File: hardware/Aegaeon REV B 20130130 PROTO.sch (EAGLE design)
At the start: 39 parts, among them IC1 ATTINY84A-MMH, Q1 DMN65D8LDW, U1 V_REG_LDOSMD

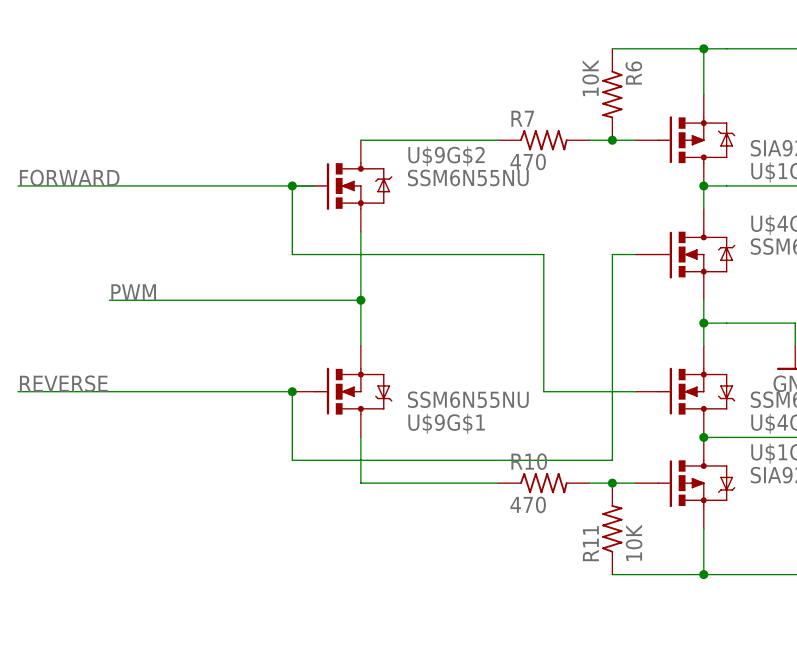
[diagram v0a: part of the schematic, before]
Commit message: Updated proto schematics to match new bridge design. Streamlined design in simulation file.
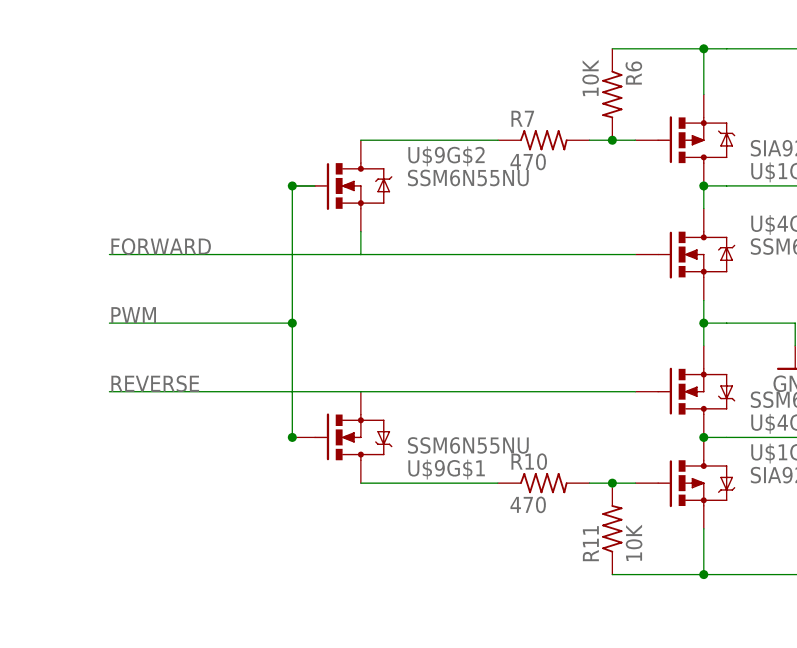
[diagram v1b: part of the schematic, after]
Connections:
- net FORWARD: now also U$4G$2.G, U$9G$2.S; no longer U$4G$1.G, U$9G$2.G
- net PWM: now also U$9G$1.G, U$9G$2.G; no longer U$9G$1.S, U$9G$2.S
- net REVERSE: now also U$4G$1.G, U$9G$1.S; no longer U$4G$2.G, U$9G$1.G
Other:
- moved on the sheet: U$9G$1
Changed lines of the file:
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@@
 <?xml version="1.0" encoding="utf-8"?>
 <!DOCTYPE eagle SYSTEM "eagle.dtd">
-<eagle version="6.1">
+<eagle version="6.5.0">
 <drawing>
 <settings>
@@
 <instance part="R11" gate="G$1" x="73.66" y="27.94" rot="R90"/>
 <instance part="U$9" gate="G$2" x="45.72" y="66.04"/>
-<instance part="U$9" gate="G$1" x="45.72" y="43.18" rot="MR180"/>
+<instance part="U$9" gate="G$1" x="45.72" y="38.1" rot="MR180"/>
 <instance part="Q1" gate="G$1" x="154.94" y="157.48"/>
 <instance part="U1" gate="G$1" x="66.04" y="111.76"/>
@@
 <net name="REVERSE" class="0">
 <segment>
-<wire x1="38.1" y1="43.18" x2="7.62" y2="43.18" width="0.1524" layer="91"/>
-<wire x1="76.2" y1="58.42" x2="73.66" y2="58.42" width="0.1524" layer="91"/>
-<wire x1="73.66" y1="58.42" x2="73.66" y2="35.56" width="0.1524" layer="91"/>
-<wire x1="73.66" y1="35.56" x2="38.1" y2="35.56" width="0.1524" layer="91"/>
-<wire x1="38.1" y1="35.56" x2="38.1" y2="43.18" width="0.1524" layer="91"/>
-<junction x="38.1" y="43.18"/>
-<pinref part="U$9" gate="G$1" pin="G"/>
-<label x="7.62" y="43.18" size="1.778" layer="95"/>
-<pinref part="U$4" gate="G$2" pin="G"/>
-</segment>
-<segment>
 <label x="109.22" y="152.4" size="1.778" layer="95"/>
 <wire x1="104.14" y1="152.4" x2="116.84" y2="152.4" width="0.1524" layer="91"/>
 <pinref part="IC1" gate="G$1" pin="PB1"/>
 </segment>
+<segment>
+<wire x1="45.72" y1="43.18" x2="17.78" y2="43.18" width="0.1524" layer="91"/>
+<label x="17.78" y="43.18" size="1.778" layer="95"/>
+<pinref part="U$9" gate="G$1" pin="S"/>
+<wire x1="76.2" y1="43.18" x2="45.72" y2="43.18" width="0.1524" layer="91"/>
+<pinref part="U$4" gate="G$1" pin="G"/>
+</segment>
 </net>
 <net name="FORWARD" class="0">
-<segment>
-<wire x1="40.64" y1="66.04" x2="38.1" y2="66.04" width="0.1524" layer="91"/>
-<wire x1="38.1" y1="66.04" x2="7.62" y2="66.04" width="0.1524" layer="91"/>
-<wire x1="76.2" y1="43.18" x2="66.04" y2="43.18" width="0.1524" layer="91"/>
-<wire x1="66.04" y1="43.18" x2="66.04" y2="58.42" width="0.1524" layer="91"/>
-<wire x1="66.04" y1="58.42" x2="38.1" y2="58.42" width="0.1524" layer="91"/>
-<wire x1="38.1" y1="58.42" x2="38.1" y2="66.04" width="0.1524" layer="91"/>
-<junction x="38.1" y="66.04"/>
-<pinref part="U$9" gate="G$2" pin="G"/>
-<label x="7.62" y="66.04" size="1.778" layer="95"/>
-<pinref part="U$4" gate="G$1" pin="G"/>
-</segment>
 <segment>
 <pinref part="IC1" gate="G$1" pin="PA7/OC0B"/>
 <wire x1="104.14" y1="160.02" x2="116.84" y2="160.02" width="0.1524" layer="91"/>
 <label x="109.22" y="160.02" size="1.778" layer="95"/>
+</segment>
+<segment>
+<wire x1="45.72" y1="58.42" x2="17.78" y2="58.42" width="0.1524" layer="91"/>
+<label x="17.78" y="58.42" size="1.778" layer="95"/>
+<pinref part="U$9" gate="G$2" pin="S"/>
+<wire x1="45.72" y1="60.96" x2="45.72" y2="58.42" width="0.1524" layer="91"/>
+<pinref part="U$4" gate="G$2" pin="G"/>
+<wire x1="45.72" y1="58.42" x2="76.2" y2="58.42" width="0.1524" layer="91"/>
 </segment>
 </net>
@@
 <wire x1="45.72" y1="33.02" x2="60.96" y2="33.02" width="0.1524" layer="91"/>
 <pinref part="U$9" gate="G$1" pin="D"/>
-<wire x1="45.72" y1="38.1" x2="45.72" y2="33.02" width="0.1524" layer="91"/>
 </segment>
 </net>
@@
 <net name="PWM" class="0">
 <segment>
-<wire x1="45.72" y1="60.96" x2="45.72" y2="53.34" width="0.1524" layer="91"/>
-<pinref part="U$9" gate="G$2" pin="S"/>
-<pinref part="U$9" gate="G$1" pin="S"/>
-<wire x1="45.72" y1="53.34" x2="45.72" y2="48.26" width="0.1524" layer="91"/>
-<wire x1="45.72" y1="53.34" x2="17.78" y2="53.34" width="0.1524" layer="91"/>
-<junction x="45.72" y="53.34"/>
-<label x="17.78" y="53.34" size="1.778" layer="95"/>
-</segment>
-<segment>
 <pinref part="IC1" gate="G$1" pin="PB2/OC0A"/>
 <wire x1="104.14" y1="157.48" x2="116.84" y2="157.48" width="0.1524" layer="91"/>
 <label x="109.22" y="157.48" size="1.778" layer="95"/>
 </segment>
-</net>
+<segment>
+<label x="17.78" y="50.8" size="1.778" layer="95"/>
+<wire x1="40.64" y1="66.04" x2="38.1" y2="66.04" width="0.1524" layer="91"/>
+<pinref part="U$9" gate="G$2" pin="G"/>
+<wire x1="17.78" y1="50.8" x2="38.1" y2="50.8" width="0.1524" layer="91"/>
+<wire x1="38.1" y1="50.8" x2="38.1" y2="66.04" width="0.1524" layer="91"/>
+<pinref part="U$9" gate="G$1" pin="G"/>
+<wire x1="38.1" y1="50.8" x2="38.1" y2="38.1" width="0.1524" layer="91"/>
+<junction x="38.1" y="50.8"/>
+<junction x="38.1" y="38.1"/>
+<junction x="38.1" y="66.04"/>
+</segment>
+</net>
